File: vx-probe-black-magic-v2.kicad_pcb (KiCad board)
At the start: 2 copper layers, 31 parts, among them P1 USB MINI B, P2 +5v power input, P3 +5v external input, P4 CONN_02X05, P5 CONN_01X04, P6 swdio/jtag, Q1 Q_PMOS_GSD, U1 stm32f070-qfp48, U2 AT45DB321D-SU, U3 TC1262-33VDB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

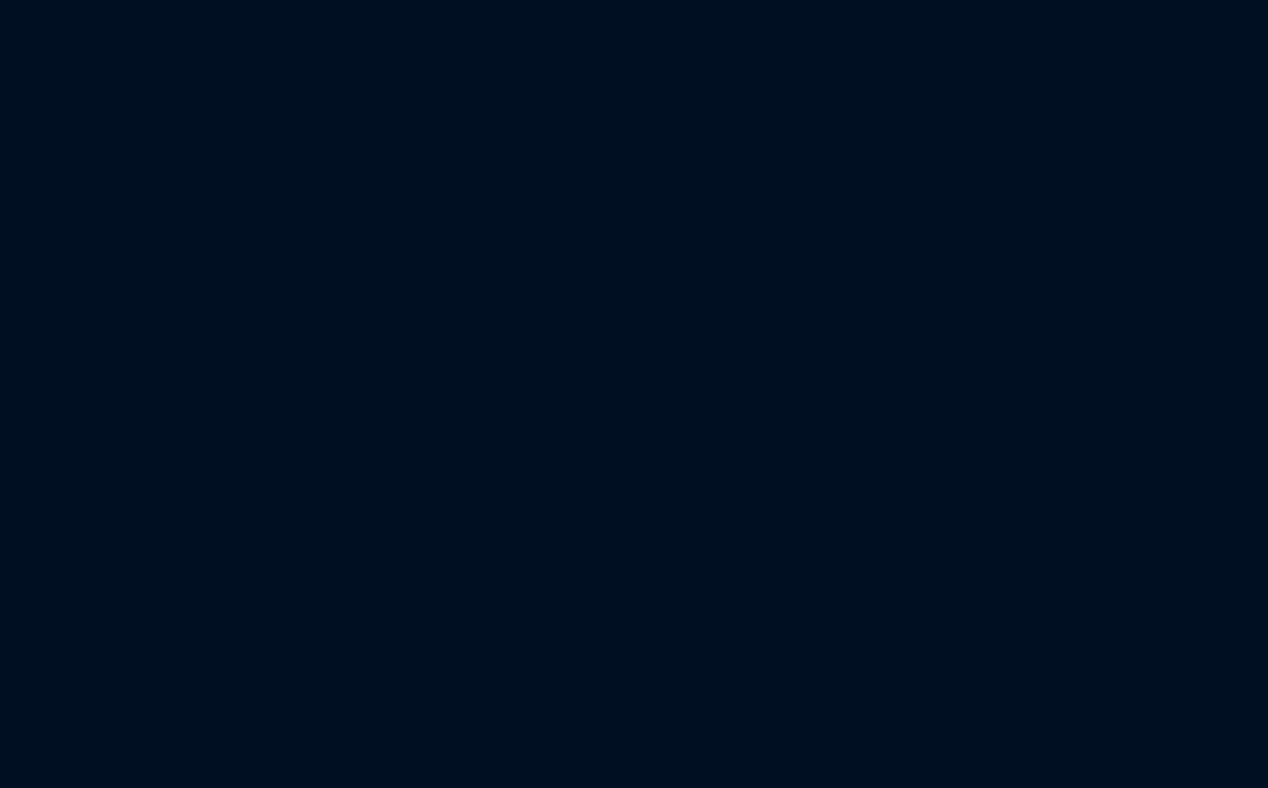
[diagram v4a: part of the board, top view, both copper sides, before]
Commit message: defined board dimensions
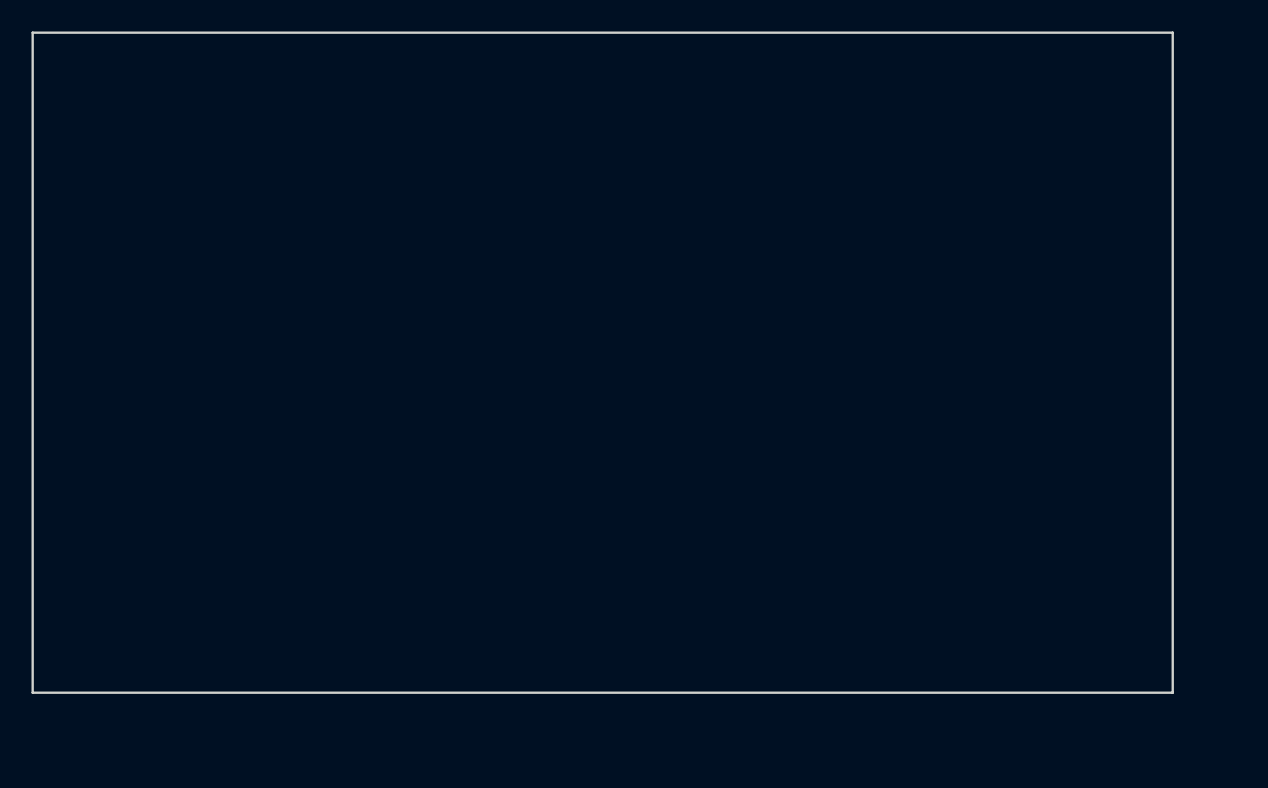
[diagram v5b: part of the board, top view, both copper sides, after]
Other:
- board outline added: 72.4 x 41.9 mm
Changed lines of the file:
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@@
     (area 20.219999 24.029999 271.880001 161.390001)
     (thickness 1.6)
-    (drawings 5)
+    (drawings 11)
     (tracks 0)
     (zones 0)
@@
       (net 3 "Net-(C2-Pad1)"))
   )
+  (gr_line (start 46.99 81.28) (end 46.99 39.37) (angle 90) (layer Edge.Cuts) (width 0.15))
+  (gr_line (start 119.38 81.28) (end 46.99 81.28) (angle 90) (layer Edge.Cuts) (width 0.15))
+  (gr_line (start 119.38 39.37) (end 119.38 81.28) (angle 90) (layer Edge.Cuts) (width 0.15))
+  (gr_line (start 46.99 39.37) (end 119.38 39.37) (angle 90) (layer Edge.Cuts) (width 0.15))
+  (dimension 72.39 (width 0.3) (layer Eco2.User)
+    (gr_text "72.390 mm" (at 83.185 32.94) (layer Eco2.User)
+      (effects (font (size 1.5 1.5) (thickness 0.3)))
+    )
+    (feature1 (pts (xy 119.38 39.37) (xy 119.38 31.59)))
+    (feature2 (pts (xy 46.99 39.37) (xy 46.99 31.59)))
+    (crossbar (pts (xy 46.99 34.29) (xy 119.38 34.29)))
+    (arrow1a (pts (xy 119.38 34.29) (xy 118.253496 34.876421)))
+    (arrow1b (pts (xy 119.38 34.29) (xy 118.253496 33.703579)))
+    (arrow2a (pts (xy 46.99 34.29) (xy 48.116504 34.876421)))
+    (arrow2b (pts (xy 46.99 34.29) (xy 48.116504 33.703579)))
+  )
+  (dimension 41.91 (width 0.3) (layer Eco2.User)
+    (gr_text "41.910 mm" (at 40.56 60.325 270) (layer Eco2.User)
+      (effects (font (size 1.5 1.5) (thickness 0.3)))
+    )
+    (feature1 (pts (xy 46.99 81.28) (xy 39.21 81.28)))
+    (feature2 (pts (xy 46.99 39.37) (xy 39.21 39.37)))
+    (crossbar (pts (xy 41.91 39.37) (xy 41.91 81.28)))
+    (arrow1a (pts (xy 41.91 81.28) (xy 41.323579 80.153496)))
+    (arrow1b (pts (xy 41.91 81.28) (xy 42.496421 80.153496)))
+    (arrow2a (pts (xy 41.91 39.37) (xy 41.323579 40.496504)))
+    (arrow2b (pts (xy 41.91 39.37) (xy 42.496421 40.496504)))
+  )
   (gr_line (start 20.32 24.13) (end 35.56 24.13) (angle 90) (layer Margin) (width 0.2))

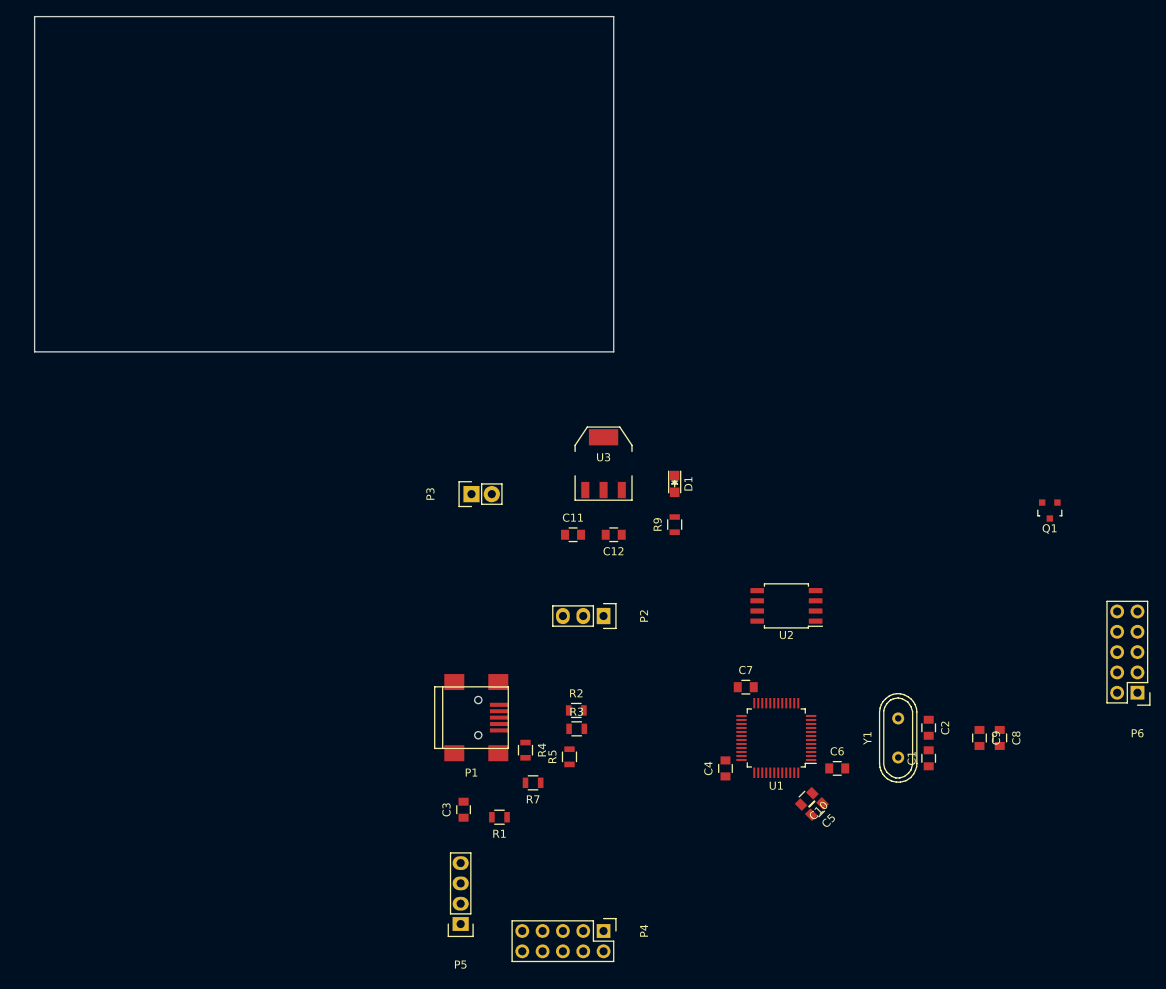
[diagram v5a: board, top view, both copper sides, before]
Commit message: started fitting the components inside the board space, autorouting to 14 vias
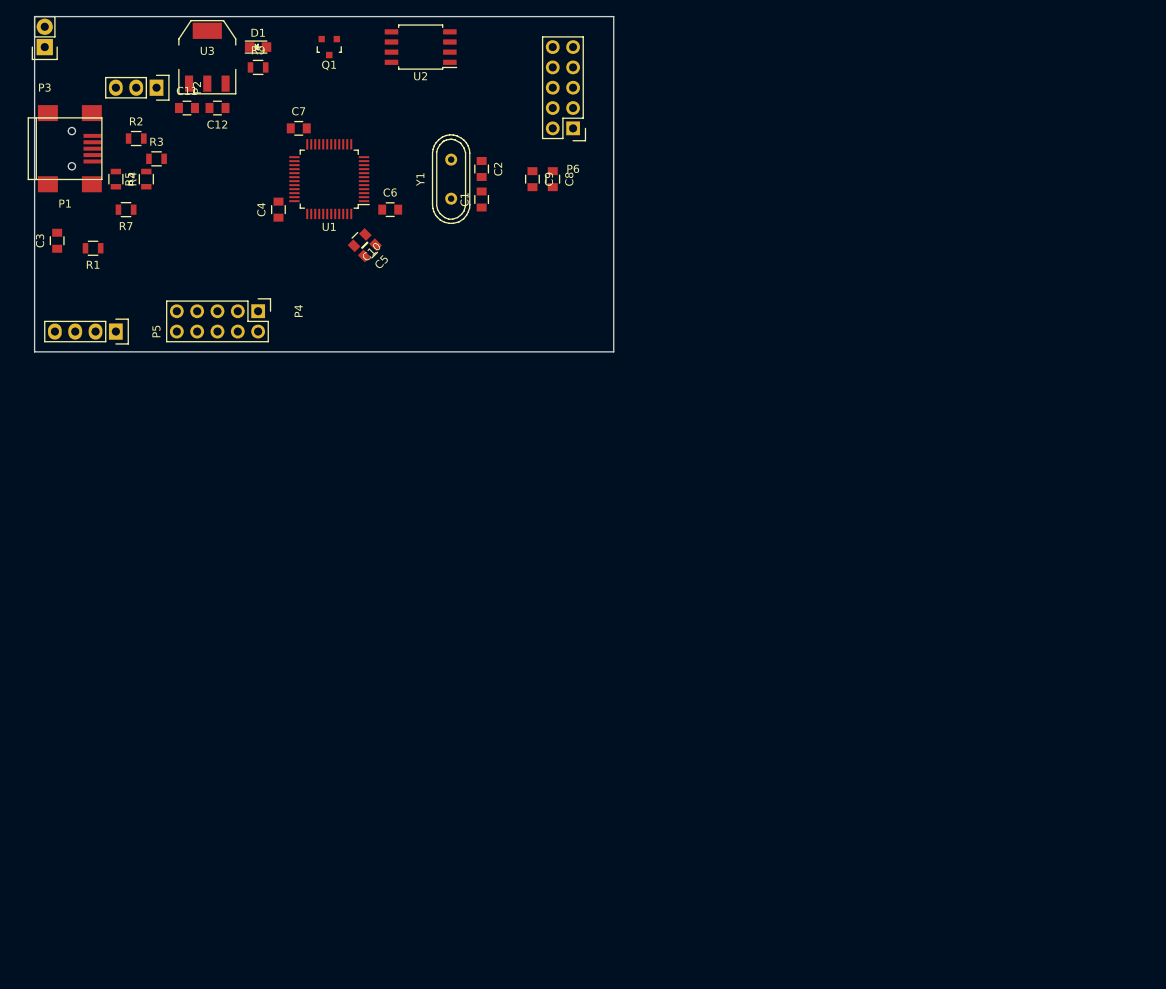
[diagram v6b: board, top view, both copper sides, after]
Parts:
- moved Q1 107.1 mm to (83.8, 43.2)
- moved P6 99.8 mm to (114.3, 53.3)
- moved R2 90.2 mm to (59.7, 54.6)
- moved R5 89.5 mm to (61.0, 59.7)
- moved C1 89.5 mm to (102.9, 62.2)
- moved C10 89.5 mm to (87.6, 67.3)
- moved C2 89.5 mm to (102.9, 58.4)
- moved C4 89.5 mm to (77.5, 63.5)
- moved C5 89.5 mm to (88.9, 68.6)
- moved C6 89.5 mm to (91.4, 63.5)
- moved C9 89.5 mm to (109.2, 59.7)
- moved U1 89.5 mm to (83.8, 59.7)
- moved Y1 89.5 mm to (99.1, 59.7)
- moved C7 89.5 mm to (80.0, 53.3)
- moved C8 89.5 mm to (111.8, 59.7)
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
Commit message: autorouting to 8 vias
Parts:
- moved R1 55.1 mm to (108.0, 55.9)
- moved P6 2.84 mm to (116.8, 52.1)
- moved P3 2.54 mm to (50.8, 43.2), turned to 90 degrees
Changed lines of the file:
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@@
   )
   (module Resistors_SMD:R_0805 (layer F.Cu)
-    (at 54.3 68.33 180)
+    (at 107.95 55.88 180)
     (descr "Resistor SMD 0805, reflow soldering, Vishay (see dcrcw.pdf)")
     (tags "resistor 0805")
@@
   )
   (module Pin_Headers:Pin_Header_Straight_1x02 (layer F.Cu)
-    (at 48.26 43.18 180)
+    (at 50.8 43.18 90)
     (descr "Through hole pin header")
     (tags "pin header")
-    (fp_text reference P3 (at 0 -5.1 180) (layer F.SilkS)
-      (effects (font (size 1 1) (thickness 0.15)))
-    )
-    (fp_text value "+5v external input" (at 0 -3.1 180) (layer F.Fab)
+    (fp_text reference P3 (at 0 -5.1 90) (layer F.SilkS)
+      (effects (font (size 1 1) (thickness 0.15)))
+    )
+    (fp_text value "+5v external input" (at 0 -3.1 90) (layer F.Fab)
       (effects (font (size 1 1) (thickness 0.15)))
     )
@@
     (fp_line (start -1.27 1.27) (end -1.27 3.81) (layer F.SilkS) (width 0.15))
     (fp_line (start -1.27 3.81) (end 1.27 3.81) (layer F.SilkS) (width 0.15))
-    (pad 1 thru_hole rect (at 0 0 180) (size 2.032 2.032) (drill 1.016) (layers *.Cu *.Mask F.SilkS)
-      (net 2 GND))
-    (pad 2 thru_hole oval (at 0 2.54 180) (size 2.032 2.032) (drill 1.016) (layers *.Cu *.Mask F.SilkS)
+    (pad 1 thru_hole rect (at 0 0 90) (size 2.032 2.032) (drill 1.016) (layers *.Cu *.Mask F.SilkS)
+      (net 2 GND))
+    (pad 2 thru_hole oval (at 0 2.54 90) (size 2.032 2.032) (drill 1.016) (layers *.Cu *.Mask F.SilkS)
       (net 23 /5V_EXT))
     (model Pin_Headers.3dshapes/Pin_Header_Straight_1x02.wrl
@@
   )
   (module Pin_Headers:Pin_Header_Straight_2x05 (layer F.Cu)
-    (at 114.3 53.34 180)
+    (at 116.84 52.07 180)
     (descr "Through hole pin header")
     (tags "pin header")

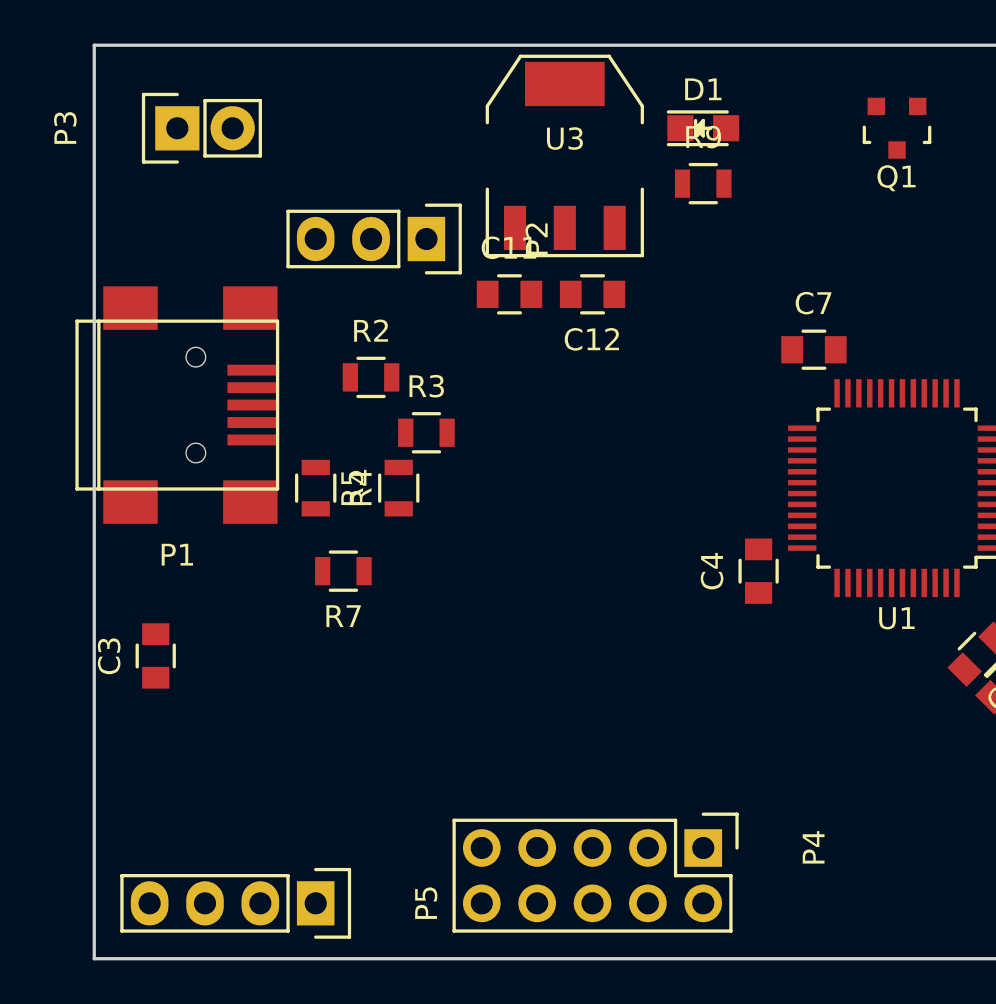
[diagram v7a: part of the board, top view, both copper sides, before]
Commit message: displaced the connectors, autorouting to 8 vias
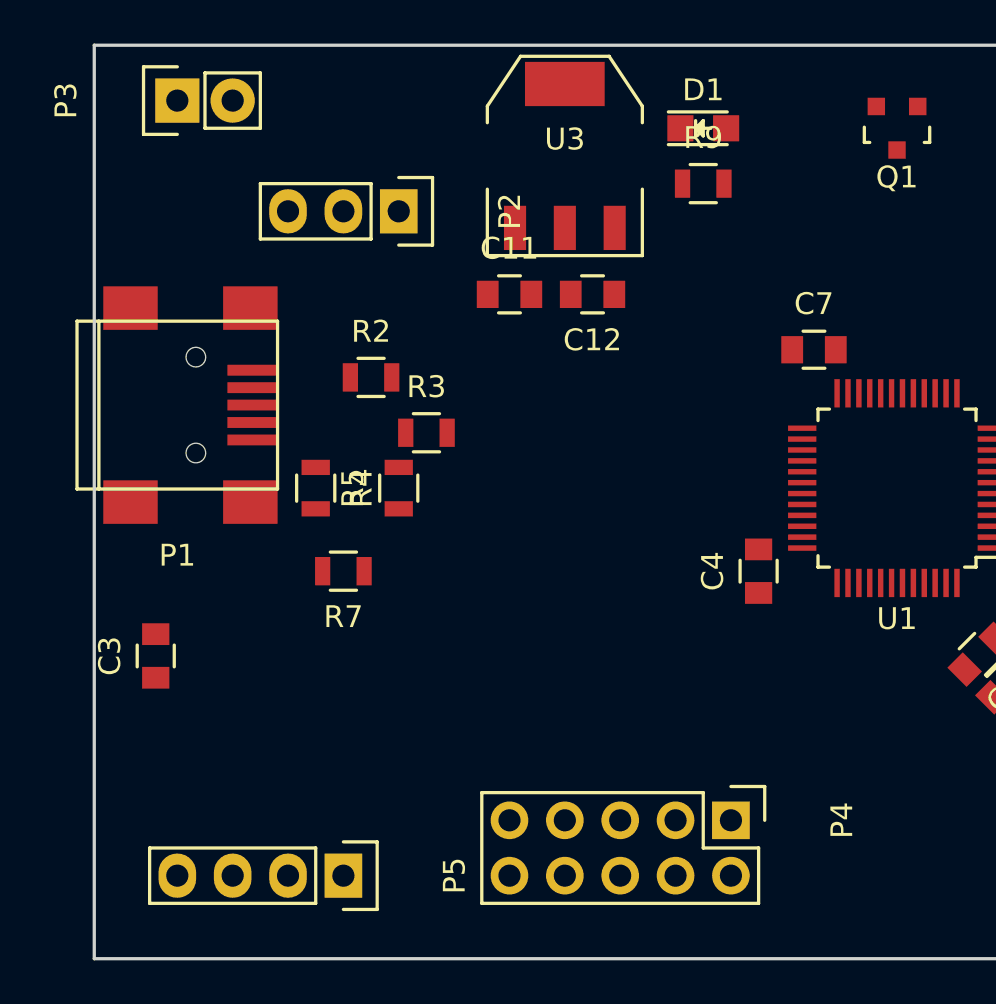
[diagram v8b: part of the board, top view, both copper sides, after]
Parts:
- moved P5 1.80 mm to (58.4, 77.5)
- moved P2 1.80 mm to (61.0, 47.0)
- moved P4 1.80 mm to (76.2, 74.9)
- moved P3 1.27 mm to (50.8, 41.9)
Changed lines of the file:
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@@
   )
   (module Pin_Headers:Pin_Header_Straight_1x03 (layer F.Cu)
-    (at 62.23 48.26 270)
+    (at 60.96 46.99 270)
     (descr "Through hole pin header")
     (tags "pin header")
@@
   )
   (module Pin_Headers:Pin_Header_Straight_1x02 (layer F.Cu)
-    (at 50.8 43.18 90)
+    (at 50.8 41.91 90)
     (descr "Through hole pin header")
     (tags "pin header")
@@
   )
   (module Pin_Headers:Pin_Header_Straight_2x05 (layer F.Cu)
-    (at 74.93 76.2 270)
+    (at 76.2 74.93 270)
     (descr "Through hole pin header")
     (tags "pin header")
@@
   )
   (module Pin_Headers:Pin_Header_Straight_1x04 (layer F.Cu)
-    (at 57.15 78.74 270)
-    (descr "Through hole pin header")
-    (tags "pin header")
+    (at 58.42 77.47 270)
+    (descr "Through hole pin header")
+    (tags "pin header")
